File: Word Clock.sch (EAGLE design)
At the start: 13 parts, among them IC1 DS3231/SO, U1 ATMEGA328P-AU

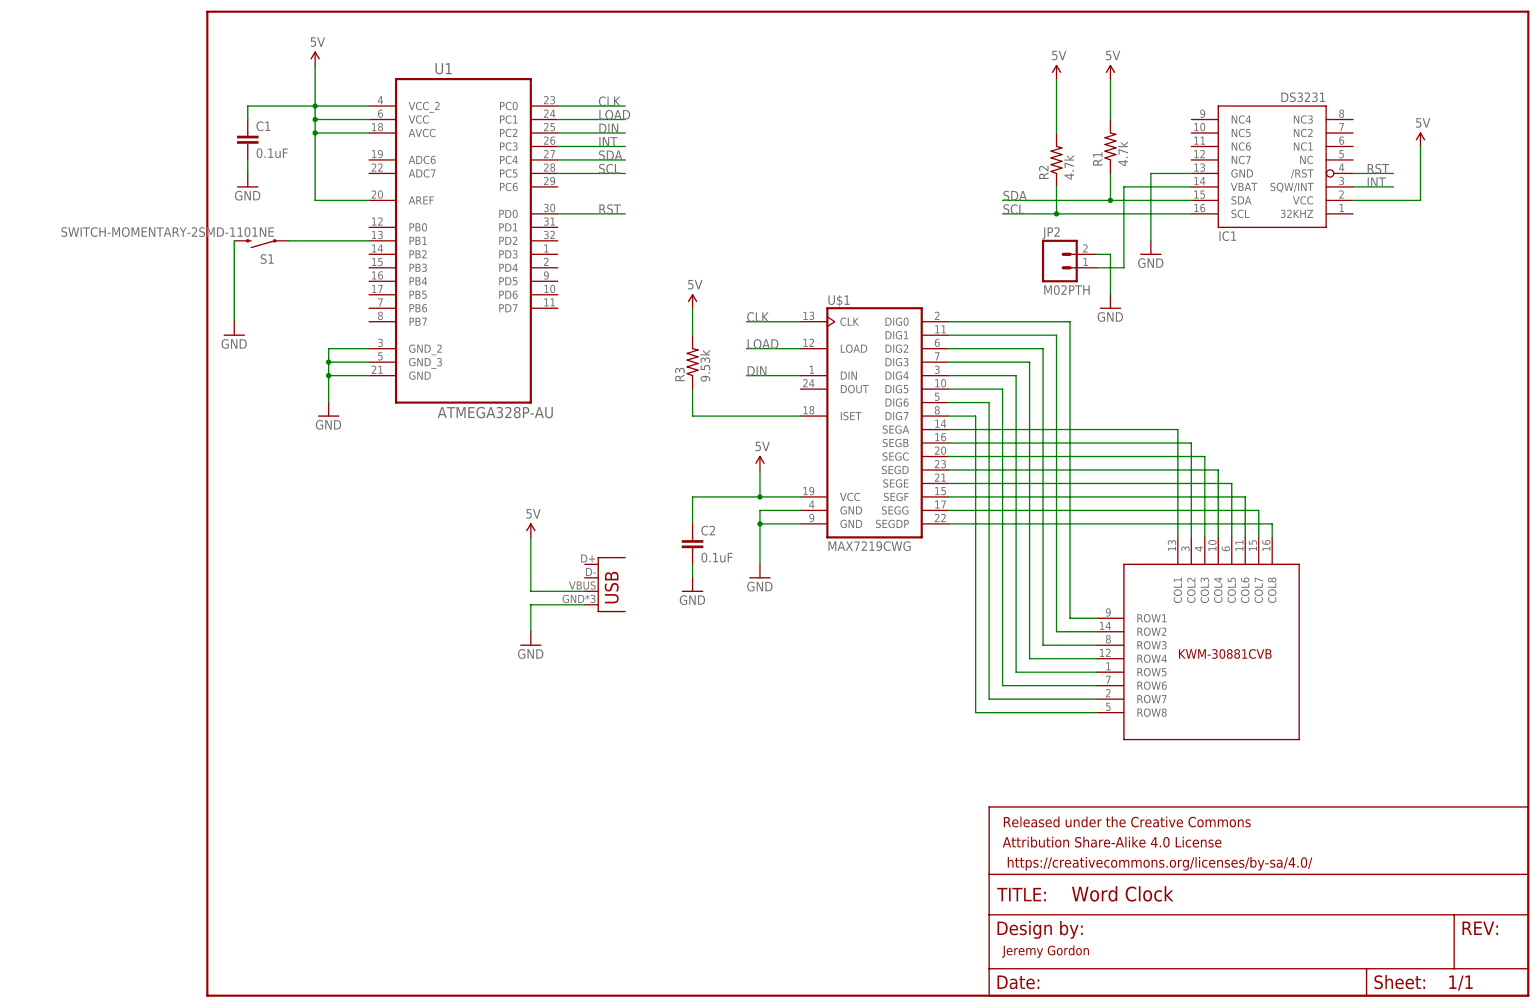
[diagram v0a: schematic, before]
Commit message: Removed MAX7219, driving with raw atmega.
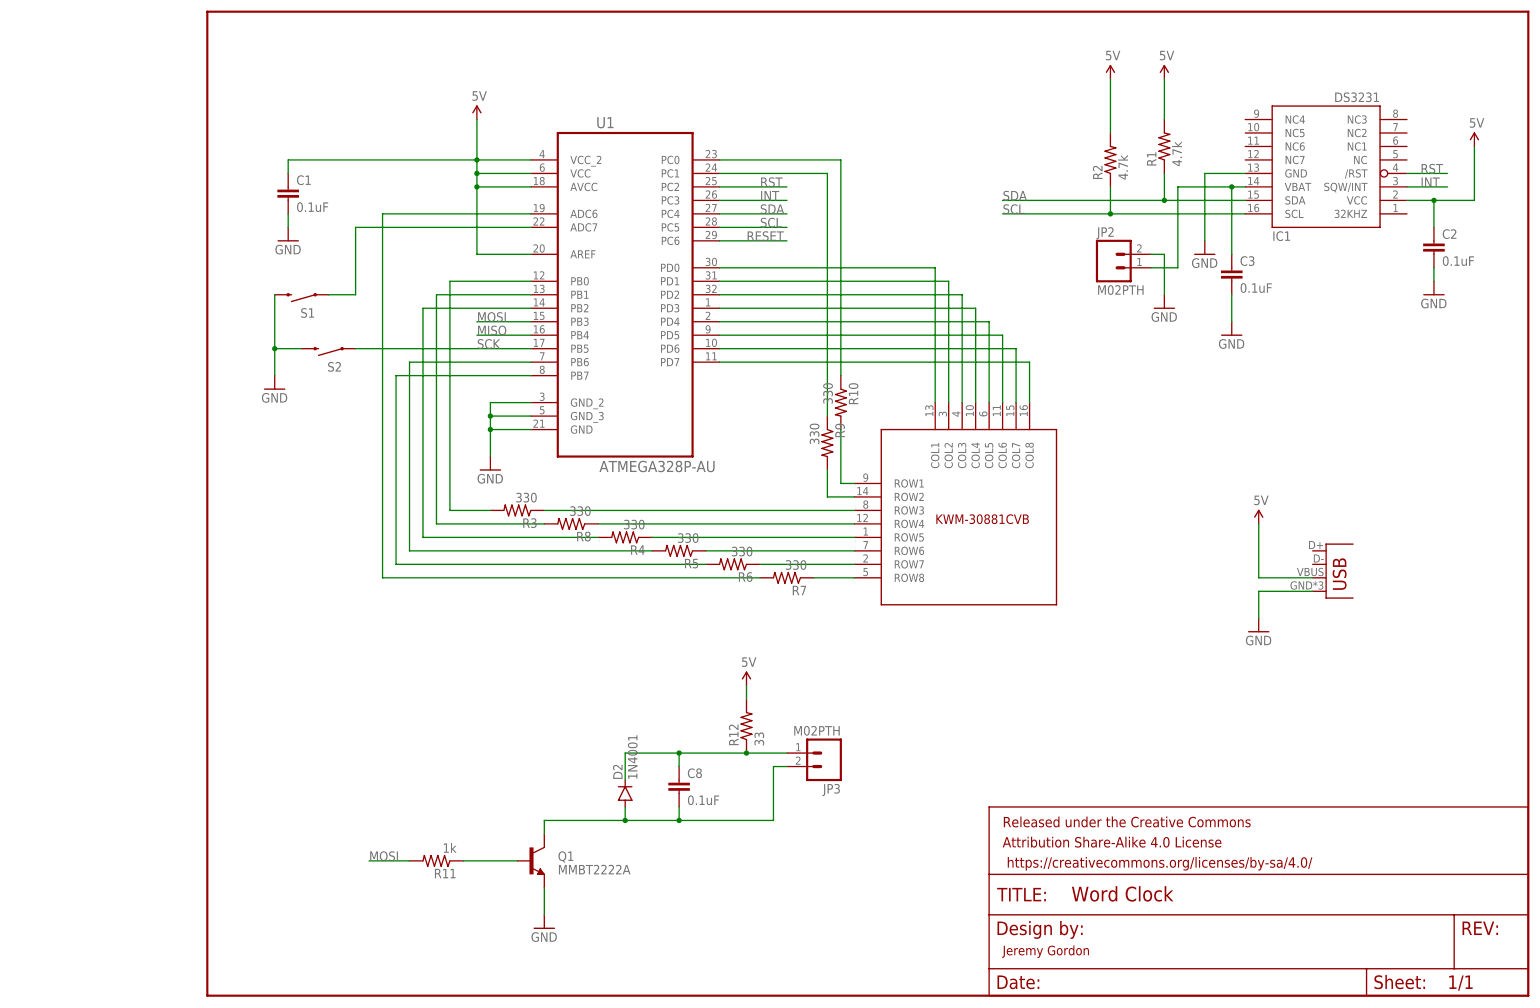
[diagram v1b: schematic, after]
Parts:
- removed U$1: MAX7219CWG, max7219:MAX7219CWG
- added C3, C8: 0.1uF, SparkFun-Capacitors:CAP0805
- added D2: 1N4001, SparkFun-DiscreteSemi:DIODESOD
- added JP3: M02PTH, SparkFun-Connectors:M02PTH
- added Q1: MMBT2222A, SparkFun-DiscreteSemi:TRANSISTOR_NPNMMBT2222A
- added R10, R4, R5, R6, R7, R8, R9: 330, SparkFun-Resistors:RESISTOR0805-RES
- added R11: 1k, SparkFun-Resistors:RESISTOR0805-RES
- added R12: 33, SparkFun-Resistors:RESISTOR0805-RES
- added S2: SWITCH-MOMENTARY-2SMD-1101NE, SparkFun-Electromechanical:SWITCH-MOMENTARY-2SMD-1101NE
- R3: value 9.53k -> 330
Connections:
- removed net CLK: U$1.CLK, U1.PC0
- removed net DIN: U$1.DIN, U1.PC2
- removed net LOAD: U$1.LOAD, U1.PC1
- new net MISO: U1.PB4
- new net MOSI: R11.2, U1.PB3
- new net N$20: D1.ROW4, R8.1
- new net N$21: D1.ROW5, R4.1
- new net N$22: D1.ROW6, R5.1
- new net N$23: D1.ROW7, R6.1
- new net N$24: D1.ROW8, R7.1
- new net N$25: D1.ROW1, R10.2
- new net N$26: D1.ROW2, R9.2
- new net N$27: Q1.B, R11.1
- new net N$28: C8.1, D2.C, JP3.1, R12.1
- new net N$29: C8.2, D2.A, JP3.2, Q1.C
- new net RESET: U1.PC6
- new net SCK: S2.1, U1.PB5
- net 5V: now also R12.2; no longer R3.2, U$1.VCC
- net GND: now also C3.2, Q1.E, S2.2; no longer U$1.GND@1, U$1.GND@2
- net N$1: now also D1.COL1, U1.PD0; no longer D1.ROW1, U$1.DIG0
- net N$10: now also R10.1, U1.PC0; no longer D1.COL2, U$1.SEGB
- net N$11: now also R3.2, U1.PB0; no longer D1.COL3, U$1.SEGC
- net N$12: now also R8.2, U1.PB1; no longer D1.COL4, U$1.SEGD
- net N$13: now also R4.2, U1.PB2; no longer D1.COL5, U$1.SEGE
- net N$14: now also R5.2, U1.PB6; no longer D1.COL6, U$1.SEGF
- net N$15: now also R6.2, U1.PB7; no longer D1.COL7, U$1.SEGG
- net N$16: now also R7.2, U1.ADC6; no longer D1.COL8, U$1.SEGDP
- net N$17: now also C3.1
- net N$18: now also S1.1, U1.ADC7; no longer R3.1, U$1.ISET
- net N$19: now also D1.ROW3, R3.1; no longer S1.1, U1.PB1
- net N$2: now also D1.COL2, U1.PD1; no longer D1.ROW2, U$1.DIG1
- net N$3: now also D1.COL3, U1.PD2; no longer D1.ROW3, U$1.DIG2
- net N$4: now also D1.COL4, U1.PD3; no longer D1.ROW4, U$1.DIG3
- net N$5: now also D1.COL5, U1.PD4; no longer D1.ROW5, U$1.DIG4
- net N$6: now also D1.COL6, U1.PD5; no longer D1.ROW6, U$1.DIG5
- net N$7: now also D1.COL7, U1.PD6; no longer D1.ROW7, U$1.DIG6
- net N$8: now also D1.COL8, U1.PD7; no longer D1.ROW8, U$1.DIG7
- net N$9: now also R9.1, U1.PC1; no longer D1.COL1, U$1.SEGA
- net RST: now also U1.PC2; no longer U1.PD0
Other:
- moved on the sheet: C1, C2, IC1, JP2, R1, R2, R3, S1, U1

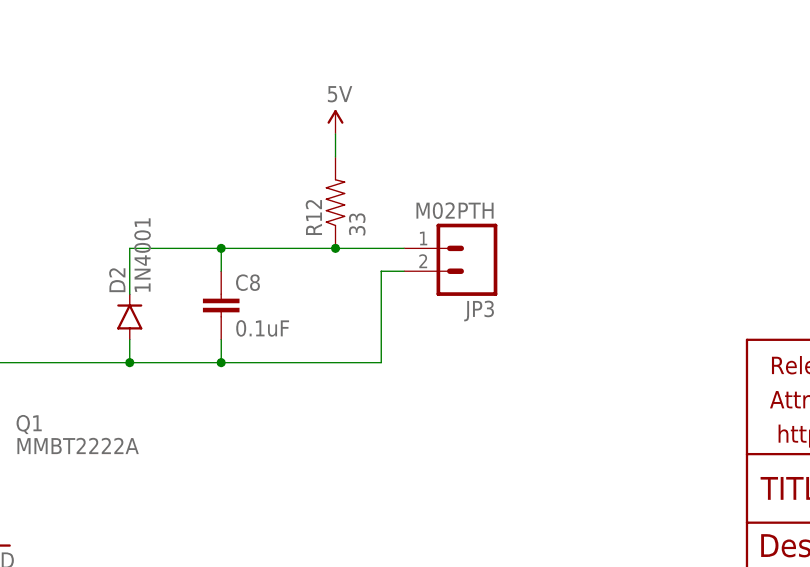
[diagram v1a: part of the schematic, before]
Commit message: Upped isloate and generally tweaked board to be more Cirqoid friendly.
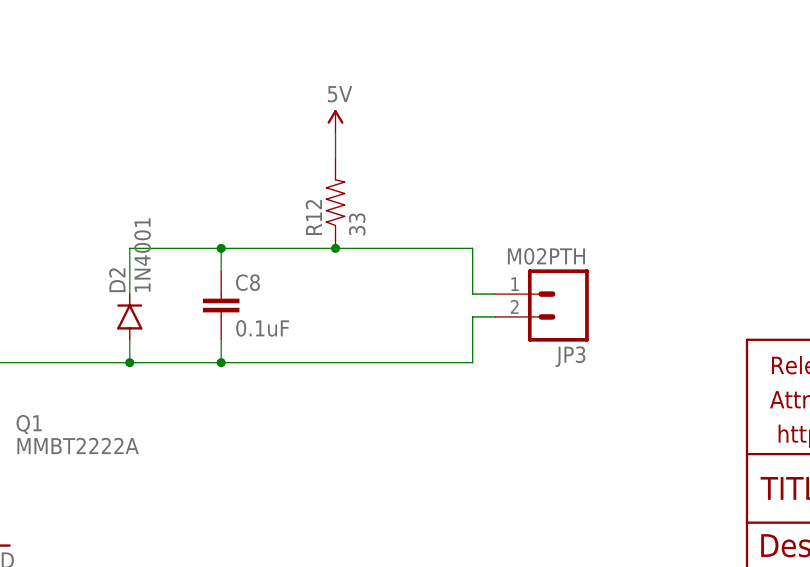
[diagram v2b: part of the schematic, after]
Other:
- moved on the sheet: JP3
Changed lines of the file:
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@@
 <instance part="GND12" gate="1" x="63.5" y="12.7"/>
 <instance part="SUPPLY5" gate="G$1" x="101.6" y="58.42"/>
-<instance part="JP3" gate="G$1" x="116.84" y="45.72" rot="R180"/>
+<instance part="JP3" gate="G$1" x="127" y="40.64" rot="R180"/>
 </instances>
 <busses>
@@
 <wire x1="78.74" y1="45.72" x2="78.74" y2="40.64" width="0.1524" layer="91"/>
 <junction x="88.9" y="45.72"/>
-<wire x1="101.6" y1="45.72" x2="109.22" y2="45.72" width="0.1524" layer="91"/>
+<wire x1="101.6" y1="45.72" x2="116.84" y2="45.72" width="0.1524" layer="91"/>
 <junction x="101.6" y="45.72"/>
+<wire x1="116.84" y1="45.72" x2="116.84" y2="40.64" width="0.1524" layer="91"/>
 <pinref part="JP3" gate="G$1" pin="1"/>
+<wire x1="116.84" y1="40.64" x2="119.38" y2="40.64" width="0.1524" layer="91"/>
 </segment>
 </net>
@@
 <wire x1="63.5" y1="33.02" x2="78.74" y2="33.02" width="0.1524" layer="91"/>
 <wire x1="78.74" y1="33.02" x2="88.9" y2="33.02" width="0.1524" layer="91"/>
-<wire x1="88.9" y1="33.02" x2="106.68" y2="33.02" width="0.1524" layer="91"/>
+<wire x1="88.9" y1="33.02" x2="116.84" y2="33.02" width="0.1524" layer="91"/>
 <pinref part="D2" gate="G$1" pin="A"/>
 <wire x1="78.74" y1="33.02" x2="78.74" y2="35.56" width="0.1524" layer="91"/>
@@
 <wire x1="88.9" y1="33.02" x2="88.9" y2="35.56" width="0.1524" layer="91"/>
 <junction x="88.9" y="33.02"/>
-<wire x1="106.68" y1="33.02" x2="106.68" y2="43.18" width="0.1524" layer="91"/>
+<wire x1="116.84" y1="33.02" x2="116.84" y2="38.1" width="0.1524" layer="91"/>
 <pinref part="JP3" gate="G$1" pin="2"/>
-<wire x1="109.22" y1="43.18" x2="106.68" y2="43.18" width="0.1524" layer="91"/>
-</segment>
-</net>
+<wire x1="116.84" y1="38.1" x2="119.38" y2="38.1" width="0.1524" layer="91"/>
+</segment>
+</net>
